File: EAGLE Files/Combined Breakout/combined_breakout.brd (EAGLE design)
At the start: 16.8 x 18.5 mm, 27 parts

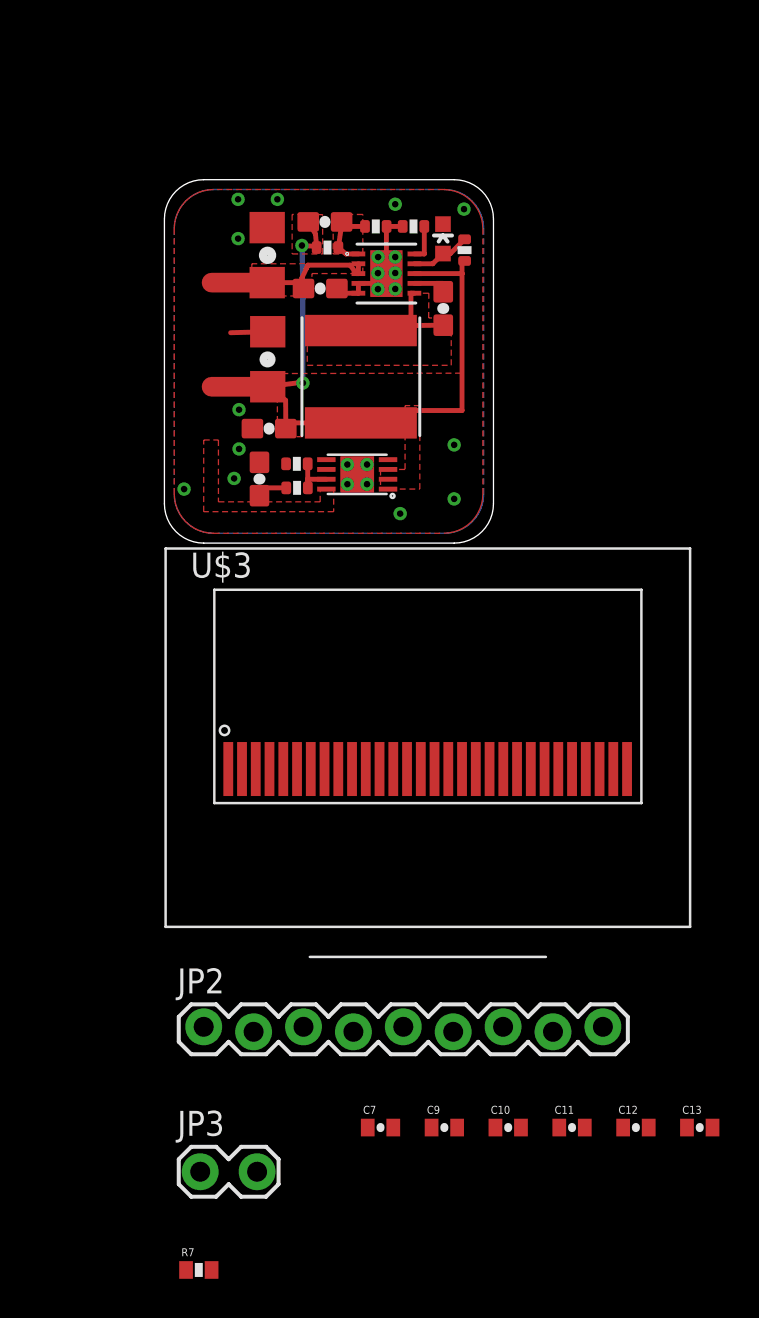
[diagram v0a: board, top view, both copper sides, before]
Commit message: Combined power/OLED breakouts. Not yet routed completely.
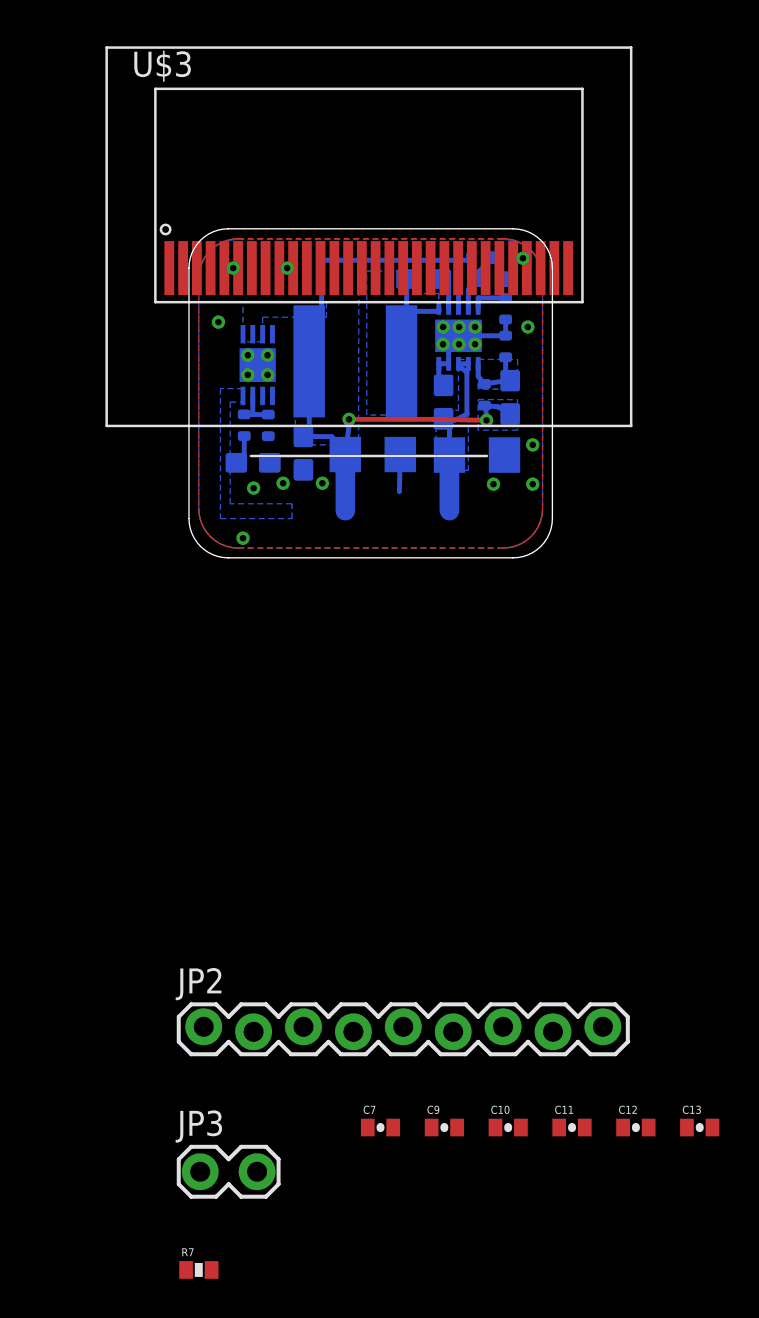
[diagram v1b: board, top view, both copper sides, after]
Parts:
- moved U$3 25.7 mm to (25.0, 35.8)
- moved C2 14.8 mm to (40.7, 26.2), flipped to the bottom, turned to 180 degrees
- moved C4 13.0 mm to (42.4, 29.2), flipped to the bottom, turned to 90 degrees
- moved R2 11.0 mm to (41.0, 29.3), flipped to the bottom, turned to 270 degrees
- moved R3 9.00 mm to (42.1, 31.8), flipped to the bottom, turned to 270 degrees
- moved C1 8.54 mm to (39.0, 28.9), flipped to the bottom, turned to 90 degrees
- moved U$2 7.52 mm to (29.5, 30.8), flipped to the bottom, turned to 270 degrees
- moved C5 7.22 mm to (35.4, 26.3), flipped to the bottom, turned to 180 degrees
- moved R1 6.29 mm to (42.1, 33.7), flipped to the bottom, turned to 90 degrees
- moved U$1 4.85 mm to (39.7, 32.3), flipped to the bottom, turned to 0 degrees
- moved R5 4.17 mm to (28.8, 27.8), flipped to the bottom, turned to 270 degrees
- moved LED1 3.29 mm to (41.5, 35.2), flipped to the bottom, turned to 90 degrees
- moved R6 2.44 mm to (30.0, 27.7), flipped to the bottom, turned to 90 degrees
- moved C6 2.15 mm to (31.8, 26.3), flipped to the bottom, turned to 270 degrees
- moved C3 1.80 mm to (37.9, 35.2), flipped to the bottom, turned to 0 degrees
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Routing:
- added copper zone on layer 16, net 3.3V
- added copper zone on layer 16, net 3.6V
- added copper zone on layer 16, net FB
- added copper zone on layer 16, net SW
- added copper zone on layer 16, net VIN
- removed copper zone on layer 1, net 3.3V
- removed copper zone on layer 1, net 3.6V
- removed copper zone on layer 1, net FB
- removed copper zone on layer 1, net SW
- removed copper zone on layer 1, net VIN
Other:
- board size 16.8 x 18.5 mm -> 18.5 x 16.8 mm

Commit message: Routing combined breakout board.
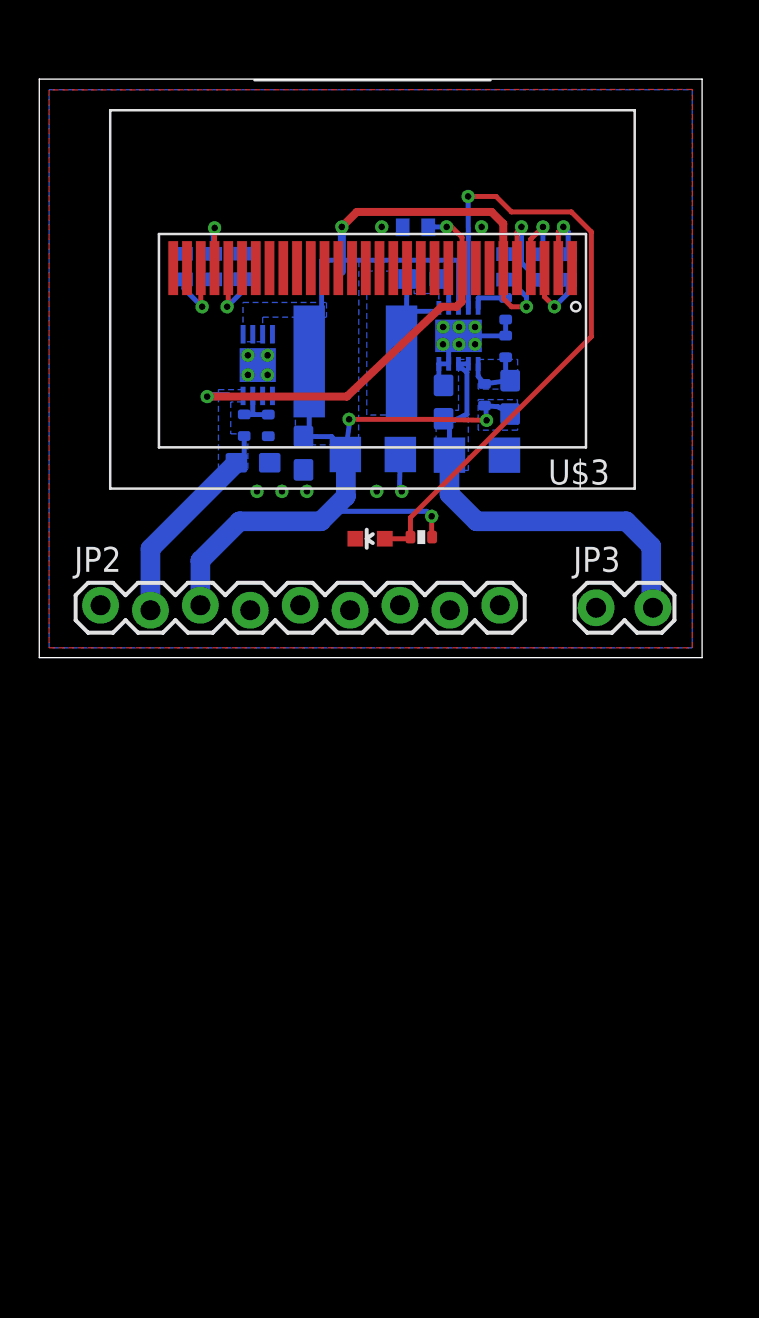
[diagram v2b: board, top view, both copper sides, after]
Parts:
- moved R7 51.1 mm to (28.7, 35.8), flipped to the bottom, turned to 270 degrees
- moved C13 50.3 mm to (27.2, 35.8), flipped to the bottom, turned to 270 degrees
- moved C12 49.5 mm to (25.7, 35.8), flipped to the bottom, turned to 90 degrees
- moved C11 46.5 mm to (37.5, 37.8), flipped to the bottom, turned to 180 degrees
- moved C7 44.8 mm to (45.3, 35.8), flipped to the bottom, turned to 270 degrees
- moved C9 44.1 mm to (43.8, 35.8), flipped to the bottom, turned to 270 degrees
- moved C10 43.8 mm to (42.1, 35.8), flipped to the bottom, turned to 90 degrees
- moved JP3 35.1 mm to (46.9, 18.5)
- moved JP2 22.1 mm to (21.5, 18.5)
- moved U$3 20.5 mm to (45.5, 35.8), turned to 180 degrees
- moved LED1 14.6 mm to (35.2, 22.0), flipped to the top
- moved R4 14.6 mm to (37.8, 22.1), flipped to the top
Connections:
- net CS#: now also JP2.9; no longer JP2.6
- net MOSI: now also JP2.5; no longer JP2.9
- net RESET: now also JP2.8; no longer JP2.5
- net SCK: now also JP2.6; no longer JP2.8
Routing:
- net 3.6V: track 35.4 -> 70.1 mm, vias 2 -> 5
- net 3.3V: track 1.76 -> 33.0 mm, vias 0 -> 2
- net N$2: track 3.07 -> 33.4 mm, vias 0 -> 1
- net VIN: track 9.41 -> 23.1 mm
- net N$9: track 0.00 -> 5.23 mm, vias 0 -> 1
- net N$8: track 0.00 -> 4.06 mm, vias 0 -> 1
- net N$11: track 0.00 -> 3.88 mm, vias 0 -> 1
- net N$1: track 0.00 -> 3.77 mm, vias 0 -> 1
- net N$5: track 0.00 -> 3.71 mm, vias 0 -> 1
- net N$12: track 0.00 -> 3.69 mm, vias 0 -> 1
- net N$3: track 0.00 -> 3.60 mm, vias 0 -> 1
- net GND: vias 22 -> 17
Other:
- board size 18.5 x 16.8 mm -> 33.7 x 29.4 mm

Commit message: Finally finished combined breakout board. It's pretty ugly but it will work for prototyping purposes.
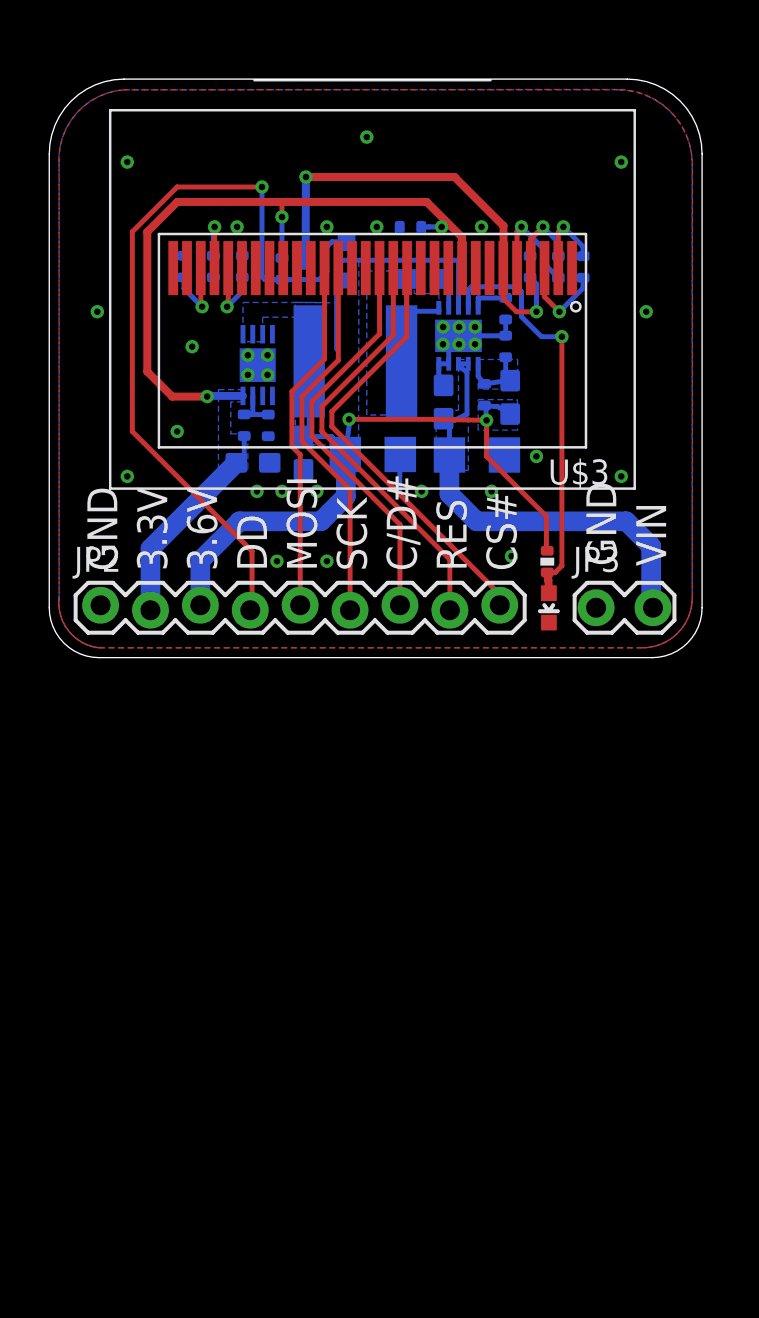
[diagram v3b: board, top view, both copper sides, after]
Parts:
- added Q1: MOSFET-PCHANNELSMD, chips:SOT23-3
- added R8: 100k, chips:0402-S
- C10, C11, C12, C13, C7, C9: device chips:0402-CAP -> chips:0402-S
- R7: device chips:0402-RES -> chips:0402-S
- moved LED1 9.76 mm to (44.3, 18.5), turned to 180 degrees
- moved R4 6.53 mm to (44.2, 20.8), turned to 90 degrees
- moved C10 1.27 mm to (43.4, 35.8)
- moved C9 1.02 mm to (44.8, 35.8)
- moved C7 0.76 mm to (46.1, 35.8)
- moved C11 0.25 mm to (37.3, 37.8)
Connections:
- new net N$15: C10.1, Q1.3, U$3.6
- net 3.3V: now also R8.2
- net 3.6V: now also Q1.2; no longer C10.1, U$3.6
- net PWR_DN: now also Q1.1, R8.1
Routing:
- net PWR_DN: track 0.00 -> 39.9 mm, vias 0 -> 1
- net N$15: track 0.00 -> 22.8 mm, vias 0 -> 2
- net CS#: track 0.00 -> 22.3 mm
- net RESET: track 0.00 -> 21.6 mm
- net C/D#: track 0.00 -> 20.4 mm
- net SCK: track 0.00 -> 19.2 mm
- net MOSI: track 0.00 -> 18.0 mm
- net 3.6V: track 70.1 -> 53.1 mm, vias 5 -> 2
- net 3.3V: track 33.0 -> 47.7 mm, vias 2 -> 3
- net N$2: track 33.4 -> 21.1 mm
- net N$11: track 3.88 -> 4.76 mm
- net GND: vias 17 -> 32
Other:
- board size 33.7 x 29.4 mm -> 33.2 x 29.4 mm
- board text added: "3.3V"
- board text added: "3.6V"
- board text added: "C/D#"
- board text added: "CS#"
- board text added: "DD"
- board text added: "GND"
- board text added: "MOSI"
- board text added: "RES"
- board text added: "SCK"
- board text added: "VIN"

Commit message: Adjusted spacing on some of the components on the combined breakout board. Removed some silkscreen that was in the way. Checked with freeDFM, sent gerbers off to circuitgraphics!
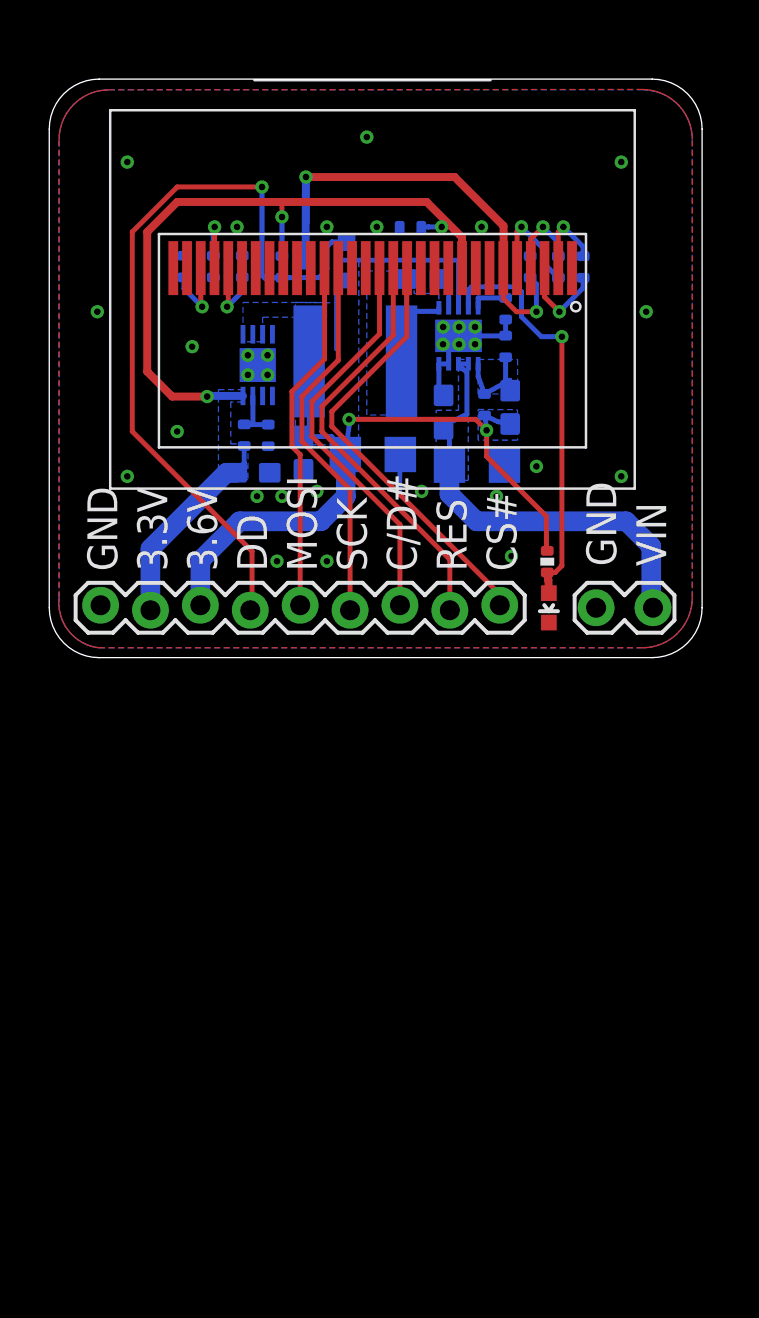
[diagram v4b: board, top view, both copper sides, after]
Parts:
- U$1: device brent:DD10 -> intelliDesk:DD10
- moved C4 0.51 mm to (42.4, 28.7)
- moved R2 0.51 mm to (41.0, 28.8)
- moved C1 0.51 mm to (39.0, 28.4)
- moved C2 0.51 mm to (40.7, 25.7)
- moved C8 0.51 mm to (29.3, 25.3)
- moved R5 0.51 mm to (28.8, 27.2)
- moved R6 0.51 mm to (30.0, 27.2)
- moved R8 0.10 mm to (30.7, 35.8)
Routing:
- net FB: track 3.86 -> 5.34 mm
- net N$6: track 2.17 -> 3.12 mm
- net 3.3V: track 47.7 -> 47.1 mm
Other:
- outline, holes or cut-outs redrawn
